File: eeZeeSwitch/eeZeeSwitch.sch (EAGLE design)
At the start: 6 parts

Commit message: Rev 0.1
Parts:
- removed SJ1: P'UP, SparkFun:SOLDERJUMPERNO
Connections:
- net N$1: now also JP1.2; no longer SJ1.1
- net N$3: no longer JP1.2, SJ1.2
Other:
- moved on the sheet: R1, S1
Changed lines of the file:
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@@
 <part name="JP1" library="pinhead-2" deviceset="PINHD-1X02" device="_2.54-S"/>
 <part name="JP2" library="pinhead-2" deviceset="PINHD-1X02" device="_2.54-S"/>
-<part name="SJ1" library="SparkFun" deviceset="SOLDERJUMPER" device="NO" value="P'UP"/>
 <part name="S1" library="bt_electromech" deviceset="SPST" device="_TAC_RECT1" value="eeZee Switch"/>
 </parts>
@@
 <instances>
 <instance part="C1" gate="G$1" x="53.34" y="40.64" rot="R90"/>
-<instance part="R1" gate="G$1" x="76.2" y="53.34"/>
+<instance part="R1" gate="G$1" x="78.74" y="53.34"/>
 <instance part="JP1" gate="A" x="106.68" y="45.72"/>
 <instance part="JP2" gate="A" x="33.02" y="45.72" rot="MR0"/>
-<instance part="SJ1" gate="1" x="76.2" y="40.64"/>
-<instance part="S1" gate="G$1" x="55.88" y="53.34"/>
+<instance part="S1" gate="G$1" x="53.34" y="53.34"/>
 </instances>
 <busses>
@@
 <segment>
 <pinref part="R1" gate="G$1" pin="1"/>
-<wire x1="60.96" y1="53.34" x2="63.5" y2="53.34" width="0.1524" layer="91"/>
-<wire x1="63.5" y1="53.34" x2="71.12" y2="53.34" width="0.1524" layer="91"/>
-<wire x1="63.5" y1="53.34" x2="63.5" y2="40.64" width="0.1524" layer="91"/>
+<wire x1="58.42" y1="53.34" x2="66.04" y2="53.34" width="0.1524" layer="91"/>
+<wire x1="66.04" y1="53.34" x2="73.66" y2="53.34" width="0.1524" layer="91"/>
+<wire x1="66.04" y1="53.34" x2="66.04" y2="40.64" width="0.1524" layer="91"/>
 <pinref part="C1" gate="G$1" pin="2"/>
-<wire x1="58.42" y1="40.64" x2="63.5" y2="40.64" width="0.1524" layer="91"/>
-<wire x1="63.5" y1="40.64" x2="71.12" y2="40.64" width="0.1524" layer="91"/>
-<pinref part="SJ1" gate="1" pin="1"/>
+<wire x1="58.42" y1="40.64" x2="66.04" y2="40.64" width="0.1524" layer="91"/>
 <pinref part="S1" gate="G$1" pin="S"/>
-<junction x="63.5" y="40.64"/>
-<junction x="63.5" y="53.34"/>
+<junction x="66.04" y="53.34"/>
+<pinref part="JP1" gate="A" pin="2"/>
+<wire x1="104.14" y1="45.72" x2="96.52" y2="45.72" width="0.1524" layer="91"/>
+<wire x1="96.52" y1="45.72" x2="96.52" y2="40.64" width="0.1524" layer="91"/>
+<wire x1="66.04" y1="40.64" x2="96.52" y2="40.64" width="0.1524" layer="91"/>
+<junction x="66.04" y="40.64"/>
 </segment>
 </net>
@@
 <wire x1="45.72" y1="40.64" x2="45.72" y2="45.72" width="0.1524" layer="91"/>
 <pinref part="JP2" gate="A" pin="1"/>
-<wire x1="50.8" y1="53.34" x2="45.72" y2="53.34" width="0.1524" layer="91"/>
+<wire x1="48.26" y1="53.34" x2="45.72" y2="53.34" width="0.1524" layer="91"/>
 <wire x1="45.72" y1="53.34" x2="45.72" y2="48.26" width="0.1524" layer="91"/>
 <wire x1="45.72" y1="48.26" x2="35.56" y2="48.26" width="0.1524" layer="91"/>
@@
 <net name="N$3" class="0">
 <segment>
-<pinref part="JP1" gate="A" pin="2"/>
-<wire x1="104.14" y1="45.72" x2="96.52" y2="45.72" width="0.1524" layer="91"/>
-<wire x1="96.52" y1="45.72" x2="96.52" y2="40.64" width="0.1524" layer="91"/>
-<wire x1="96.52" y1="40.64" x2="81.28" y2="40.64" width="0.1524" layer="91"/>
-<pinref part="SJ1" gate="1" pin="2"/>
 <pinref part="JP1" gate="A" pin="1"/>
 <pinref part="R1" gate="G$1" pin="2"/>
-<wire x1="81.28" y1="53.34" x2="96.52" y2="53.34" width="0.1524" layer="91"/>
+<wire x1="83.82" y1="53.34" x2="96.52" y2="53.34" width="0.1524" layer="91"/>
 <wire x1="96.52" y1="53.34" x2="96.52" y2="48.26" width="0.1524" layer="91"/>
 <wire x1="96.52" y1="48.26" x2="104.14" y2="48.26" width="0.1524" layer="91"/>
-<wire x1="96.52" y1="45.72" x2="96.52" y2="48.26" width="0.1524" layer="91"/>
-<junction x="96.52" y="48.26"/>
-<junction x="96.52" y="45.72"/>
 </segment>
 </net>

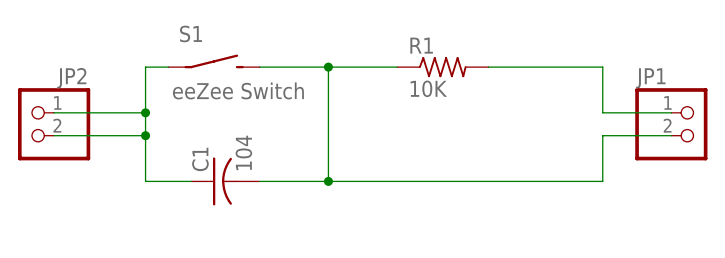
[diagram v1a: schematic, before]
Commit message: Added debounce solder jumper so switch can be used as reset. Moved components and silkscreen around to accommodate.
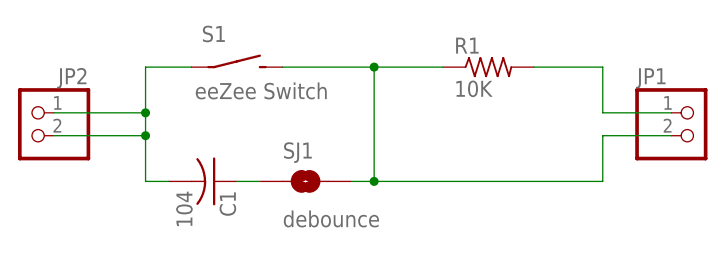
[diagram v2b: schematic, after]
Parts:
- added SJ1: debounce, SparkFun:SOLDERJUMPERNO
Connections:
- new net N$4: C1.1, SJ1.1
- net N$1: now also SJ1.2; no longer C1.2
- net N$2: now also C1.2; no longer C1.1
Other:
- moved on the sheet: C1, R1, S1
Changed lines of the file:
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@@
 <part name="JP2" library="pinhead-2" deviceset="PINHD-1X02" device="_2.54-S"/>
 <part name="S1" library="bt_electromech" deviceset="SPST" device="_TAC_RECT1" value="eeZee Switch"/>
+<part name="SJ1" library="SparkFun" deviceset="SOLDERJUMPER" device="NO" value="debounce"/>
 </parts>
 <sheets>
@@
 </plain>
 <instances>
-<instance part="C1" gate="G$1" x="53.34" y="40.64" rot="R90"/>
-<instance part="R1" gate="G$1" x="78.74" y="53.34"/>
+<instance part="C1" gate="G$1" x="53.34" y="40.64" rot="R270"/>
+<instance part="R1" gate="G$1" x="83.82" y="53.34"/>
 <instance part="JP1" gate="A" x="106.68" y="45.72"/>
 <instance part="JP2" gate="A" x="33.02" y="45.72" rot="MR0"/>
-<instance part="S1" gate="G$1" x="53.34" y="53.34"/>
+<instance part="S1" gate="G$1" x="55.88" y="53.34"/>
+<instance part="SJ1" gate="1" x="63.5" y="40.64"/>
 </instances>
 <busses>
@@
 <segment>
 <pinref part="R1" gate="G$1" pin="1"/>
-<wire x1="58.42" y1="53.34" x2="66.04" y2="53.34" width="0.1524" layer="91"/>
-<wire x1="66.04" y1="53.34" x2="73.66" y2="53.34" width="0.1524" layer="91"/>
-<wire x1="66.04" y1="53.34" x2="66.04" y2="40.64" width="0.1524" layer="91"/>
-<pinref part="C1" gate="G$1" pin="2"/>
-<wire x1="58.42" y1="40.64" x2="66.04" y2="40.64" width="0.1524" layer="91"/>
+<wire x1="60.96" y1="53.34" x2="71.12" y2="53.34" width="0.1524" layer="91"/>
+<wire x1="71.12" y1="53.34" x2="78.74" y2="53.34" width="0.1524" layer="91"/>
+<wire x1="71.12" y1="53.34" x2="71.12" y2="40.64" width="0.1524" layer="91"/>
 <pinref part="S1" gate="G$1" pin="S"/>
-<junction x="66.04" y="53.34"/>
+<junction x="71.12" y="53.34"/>
 <pinref part="JP1" gate="A" pin="2"/>
 <wire x1="104.14" y1="45.72" x2="96.52" y2="45.72" width="0.1524" layer="91"/>
 <wire x1="96.52" y1="45.72" x2="96.52" y2="40.64" width="0.1524" layer="91"/>
-<wire x1="66.04" y1="40.64" x2="96.52" y2="40.64" width="0.1524" layer="91"/>
-<junction x="66.04" y="40.64"/>
+<wire x1="71.12" y1="40.64" x2="96.52" y2="40.64" width="0.1524" layer="91"/>
+<pinref part="SJ1" gate="1" pin="2"/>
+<wire x1="68.58" y1="40.64" x2="71.12" y2="40.64" width="0.1524" layer="91"/>
+<junction x="71.12" y="40.64"/>
 </segment>
 </net>
@@
 <junction x="45.72" y="45.72"/>
 <wire x1="45.72" y1="45.72" x2="35.56" y2="45.72" width="0.1524" layer="91"/>
-<pinref part="C1" gate="G$1" pin="1"/>
-<wire x1="50.8" y1="40.64" x2="45.72" y2="40.64" width="0.1524" layer="91"/>
 <wire x1="45.72" y1="40.64" x2="45.72" y2="45.72" width="0.1524" layer="91"/>
 <pinref part="JP2" gate="A" pin="1"/>
-<wire x1="48.26" y1="53.34" x2="45.72" y2="53.34" width="0.1524" layer="91"/>
+<wire x1="50.8" y1="53.34" x2="45.72" y2="53.34" width="0.1524" layer="91"/>
 <wire x1="45.72" y1="53.34" x2="45.72" y2="48.26" width="0.1524" layer="91"/>
 <wire x1="45.72" y1="48.26" x2="35.56" y2="48.26" width="0.1524" layer="91"/>
@@
 <junction x="45.72" y="48.26"/>
 <pinref part="S1" gate="G$1" pin="P"/>
+<pinref part="C1" gate="G$1" pin="2"/>
+<wire x1="48.26" y1="40.64" x2="45.72" y2="40.64" width="0.1524" layer="91"/>
 </segment>
 </net>
@@
 <pinref part="JP1" gate="A" pin="1"/>
 <pinref part="R1" gate="G$1" pin="2"/>
-<wire x1="83.82" y1="53.34" x2="96.52" y2="53.34" width="0.1524" layer="91"/>
+<wire x1="88.9" y1="53.34" x2="96.52" y2="53.34" width="0.1524" layer="91"/>
 <wire x1="96.52" y1="53.34" x2="96.52" y2="48.26" width="0.1524" layer="91"/>
 <wire x1="96.52" y1="48.26" x2="104.14" y2="48.26" width="0.1524" layer="91"/>
 </segment>
 </net>
+<net name="N$4" class="0">
+<segment>
+<pinref part="SJ1" gate="1" pin="1"/>
+<pinref part="C1" gate="G$1" pin="1"/>
+<wire x1="55.88" y1="40.64" x2="58.42" y2="40.64" width="0.1524" layer="91"/>
+</segment>
+</net>

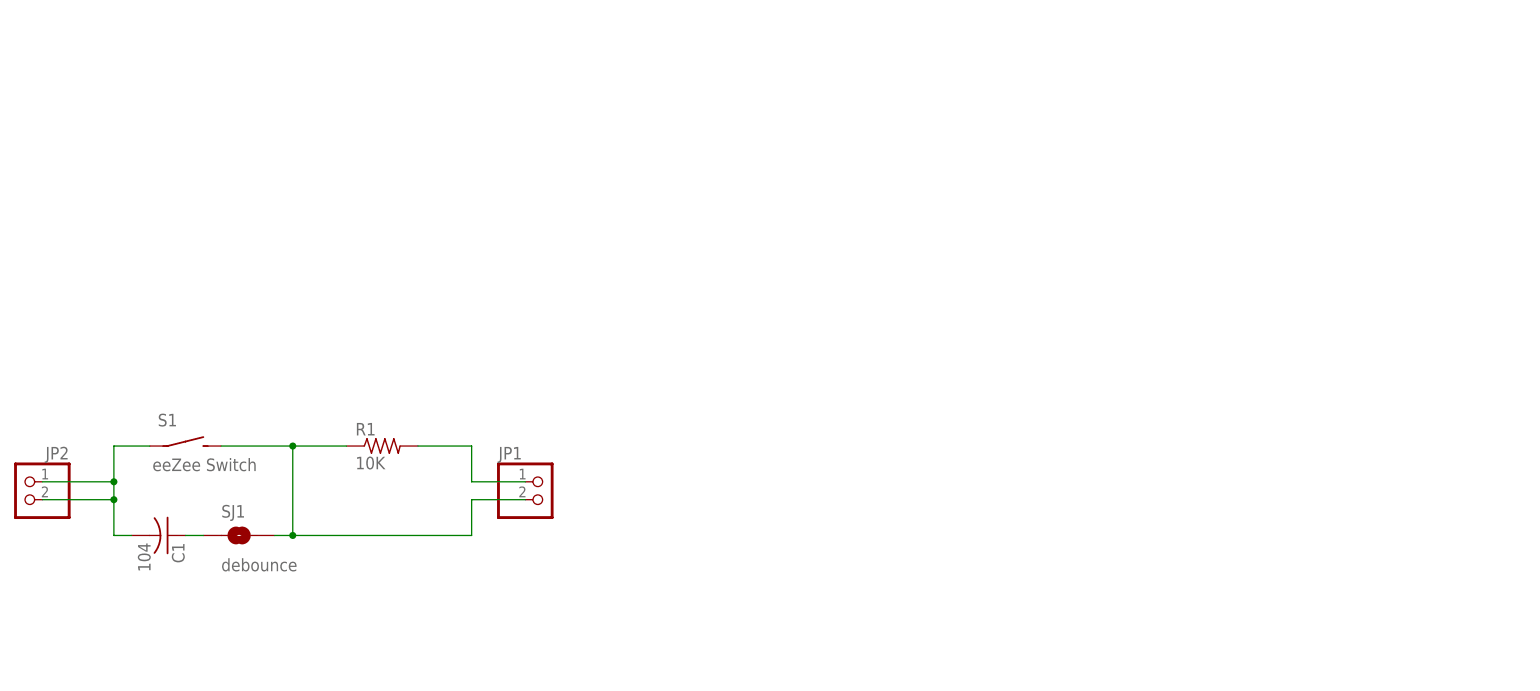
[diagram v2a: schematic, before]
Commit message: Revised circuit for easier optional debounce, revised silk for better usability.
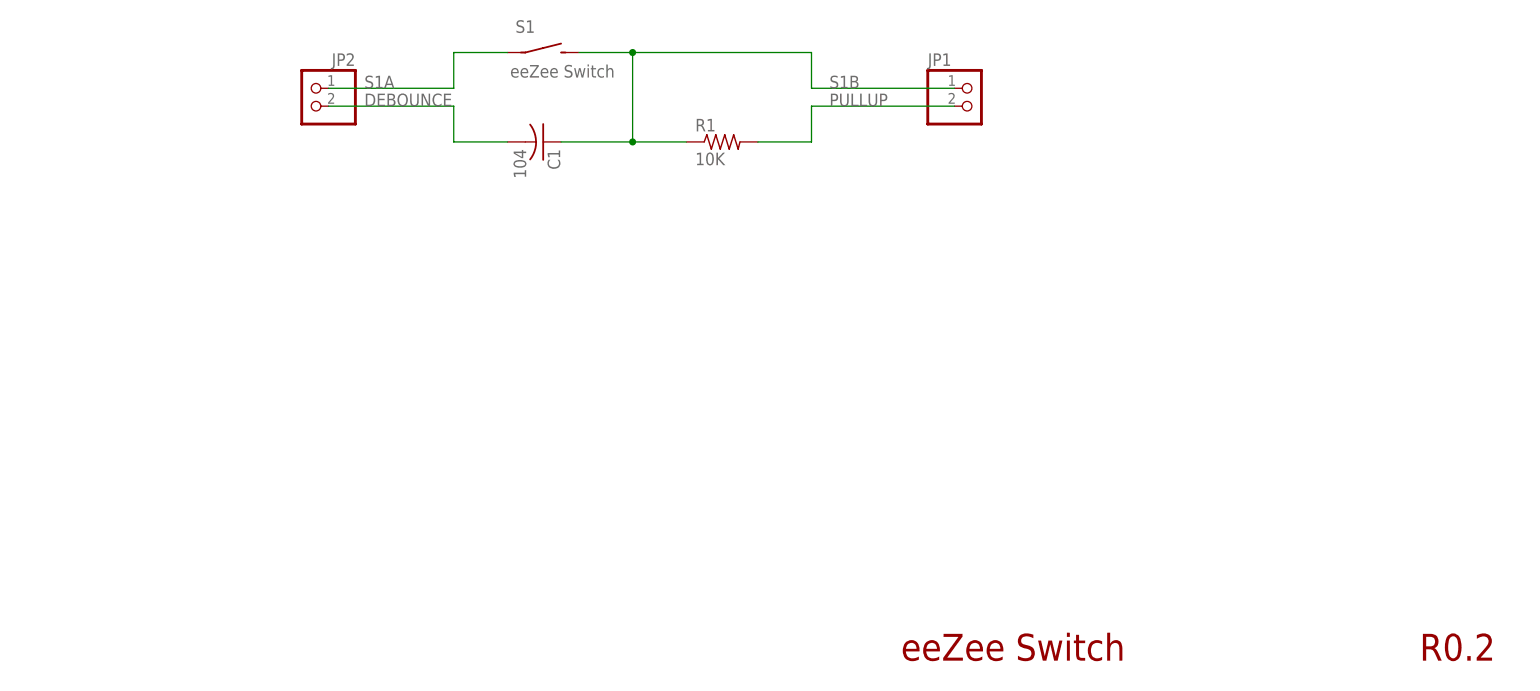
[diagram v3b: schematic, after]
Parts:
- removed SJ1: debounce, SparkFun:SOLDERJUMPERNO
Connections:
- removed net N$1: JP1.2, R1.1, S1.S, SJ1.2
- removed net N$2: C1.2, JP2.1, JP2.2, S1.P
- removed net N$3: JP1.1, R1.2
- removed net N$4: C1.1, SJ1.1
- new net DEBOUNCE: C1.2, JP2.2
- new net PULLUP: JP1.2, R1.2
- new net S1A: JP2.1, S1.P
- new net S1B: C1.1, JP1.1, R1.1, S1.S
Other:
- note added: "R0.2"
- note added: "eeZee Switch"
- moved on the sheet: C1, JP1, JP2, R1, S1
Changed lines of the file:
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@@
 <part name="JP2" library="pinhead-2" deviceset="PINHD-1X02" device="_2.54-S"/>
 <part name="S1" library="bt_electromech" deviceset="SPST" device="_TAC_RECT1" value="eeZee Switch"/>
-<part name="SJ1" library="SparkFun" deviceset="SOLDERJUMPER" device="NO" value="debounce"/>
+<part name="FRAME1" library="bt" deviceset="LETTER_L" device=""/>
 </parts>
 <sheets>
 <sheet>
 <plain>
+<text x="157.48" y="22.86" size="3.81" layer="94">eeZee Switch</text>
+<text x="231.14" y="22.86" size="3.81" layer="94">R0.2</text>
 </plain>
 <instances>
-<instance part="C1" gate="G$1" x="53.34" y="40.64" rot="R270"/>
-<instance part="R1" gate="G$1" x="83.82" y="53.34"/>
-<instance part="JP1" gate="A" x="106.68" y="45.72"/>
-<instance part="JP2" gate="A" x="33.02" y="45.72" rot="MR0"/>
-<instance part="S1" gate="G$1" x="55.88" y="53.34"/>
-<instance part="SJ1" gate="1" x="63.5" y="40.64"/>
+<instance part="C1" gate="G$1" x="106.68" y="96.52" rot="R270"/>
+<instance part="R1" gate="G$1" x="132.08" y="96.52"/>
+<instance part="JP1" gate="A" x="167.64" y="101.6"/>
+<instance part="JP2" gate="A" x="73.66" y="101.6" rot="MR0"/>
+<instance part="S1" gate="G$1" x="106.68" y="109.22"/>
+<instance part="FRAME1" gate="G$1" x="0" y="0"/>
+<instance part="FRAME1" gate="G$2" x="147.32" y="2.54"/>
 </instances>
 <busses>
 </busses>
 <nets>
-<net name="N$1" class="0">
+<net name="S1A" class="0">
 <segment>
-<pinref part="R1" gate="G$1" pin="1"/>
-<wire x1="60.96" y1="53.34" x2="71.12" y2="53.34" width="0.1524" layer="91"/>
-<wire x1="71.12" y1="53.34" x2="78.74" y2="53.34" width="0.1524" layer="91"/>
-<wire x1="71.12" y1="53.34" x2="71.12" y2="40.64" width="0.1524" layer="91"/>
-<pinref part="S1" gate="G$1" pin="S"/>
-<junction x="71.12" y="53.34"/>
-<pinref part="JP1" gate="A" pin="2"/>
-<wire x1="104.14" y1="45.72" x2="96.52" y2="45.72" width="0.1524" layer="91"/>
-<wire x1="96.52" y1="45.72" x2="96.52" y2="40.64" width="0.1524" layer="91"/>
-<wire x1="71.12" y1="40.64" x2="96.52" y2="40.64" width="0.1524" layer="91"/>
-<pinref part="SJ1" gate="1" pin="2"/>
-<wire x1="68.58" y1="40.64" x2="71.12" y2="40.64" width="0.1524" layer="91"/>
-<junction x="71.12" y="40.64"/>
+<pinref part="JP2" gate="A" pin="1"/>
+<wire x1="101.6" y1="109.22" x2="93.98" y2="109.22" width="0.1524" layer="91"/>
+<wire x1="93.98" y1="109.22" x2="93.98" y2="104.14" width="0.1524" layer="91"/>
+<wire x1="93.98" y1="104.14" x2="76.2" y2="104.14" width="0.1524" layer="91"/>
+<pinref part="S1" gate="G$1" pin="P"/>
+<label x="81.28" y="104.14" size="1.778" layer="95"/>
 </segment>
 </net>
-<net name="N$2" class="0">
+<net name="S1B" class="0">
+<segment>
+<pinref part="C1" gate="G$1" pin="1"/>
+<wire x1="111.76" y1="109.22" x2="119.38" y2="109.22" width="0.1524" layer="91"/>
+<wire x1="119.38" y1="109.22" x2="119.38" y2="96.52" width="0.1524" layer="91"/>
+<pinref part="S1" gate="G$1" pin="S"/>
+<wire x1="109.22" y1="96.52" x2="119.38" y2="96.52" width="0.1524" layer="91"/>
+<pinref part="JP1" gate="A" pin="1"/>
+<wire x1="144.78" y1="109.22" x2="144.78" y2="104.14" width="0.1524" layer="91"/>
+<wire x1="144.78" y1="104.14" x2="165.1" y2="104.14" width="0.1524" layer="91"/>
+<wire x1="119.38" y1="109.22" x2="144.78" y2="109.22" width="0.1524" layer="91"/>
+<label x="147.32" y="104.14" size="1.778" layer="95"/>
+<pinref part="R1" gate="G$1" pin="1"/>
+<wire x1="119.38" y1="96.52" x2="127" y2="96.52" width="0.1524" layer="91"/>
+<junction x="119.38" y="109.22"/>
+<junction x="119.38" y="96.52"/>
+</segment>
+</net>
+<net name="DEBOUNCE" class="0">
 <segment>
 <pinref part="JP2" gate="A" pin="2"/>
-<junction x="45.72" y="45.72"/>
-<wire x1="45.72" y1="45.72" x2="35.56" y2="45.72" width="0.1524" layer="91"/>
-<wire x1="45.72" y1="40.64" x2="45.72" y2="45.72" width="0.1524" layer="91"/>
-<pinref part="JP2" gate="A" pin="1"/>
-<wire x1="50.8" y1="53.34" x2="45.72" y2="53.34" width="0.1524" layer="91"/>
-<wire x1="45.72" y1="53.34" x2="45.72" y2="48.26" width="0.1524" layer="91"/>
-<wire x1="45.72" y1="48.26" x2="35.56" y2="48.26" width="0.1524" layer="91"/>
-<wire x1="45.72" y1="45.72" x2="45.72" y2="48.26" width="0.1524" layer="91"/>
-<junction x="45.72" y="48.26"/>
-<pinref part="S1" gate="G$1" pin="P"/>
 <pinref part="C1" gate="G$1" pin="2"/>
-<wire x1="48.26" y1="40.64" x2="45.72" y2="40.64" width="0.1524" layer="91"/>
+<wire x1="101.6" y1="96.52" x2="93.98" y2="96.52" width="0.1524" layer="91"/>
+<wire x1="93.98" y1="96.52" x2="93.98" y2="101.6" width="0.1524" layer="91"/>
+<wire x1="93.98" y1="101.6" x2="76.2" y2="101.6" width="0.1524" layer="91"/>
+<label x="81.28" y="101.6" size="1.778" layer="95"/>
 </segment>
 </net>
-<net name="N$3" class="0">
+<net name="PULLUP" class="0">
 <segment>
-<pinref part="JP1" gate="A" pin="1"/>
+<pinref part="JP1" gate="A" pin="2"/>
+<wire x1="165.1" y1="101.6" x2="144.78" y2="101.6" width="0.1524" layer="91"/>
+<wire x1="144.78" y1="101.6" x2="144.78" y2="96.52" width="0.1524" layer="91"/>
+<label x="147.32" y="101.6" size="1.778" layer="95"/>
 <pinref part="R1" gate="G$1" pin="2"/>
-<wire x1="88.9" y1="53.34" x2="96.52" y2="53.34" width="0.1524" layer="91"/>
-<wire x1="96.52" y1="53.34" x2="96.52" y2="48.26" width="0.1524" layer="91"/>
-<wire x1="96.52" y1="48.26" x2="104.14" y2="48.26" width="0.1524" layer="91"/>
+<wire x1="137.16" y1="96.52" x2="144.78" y2="96.52" width="0.1524" layer="91"/>
 </segment>
 </net>
-<net name="N$4" class="0">
-<segment>
-<pinref part="SJ1" gate="1" pin="1"/>
-<pinref part="C1" gate="G$1" pin="1"/>
-<wire x1="55.88" y1="40.64" x2="58.42" y2="40.64" width="0.1524" layer="91"/>
-</segment>
-</net>
